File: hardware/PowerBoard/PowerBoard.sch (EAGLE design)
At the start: 136 parts, among them J1 CON-HRS-DM3AT, J2 CON-ZX62R-B-5P, J3 CON-FTSH-105-01-L-DV-K, J4 CON-S2B-PH-SM4-TB, J5 CON-PJ-102A, J6 CON-71436-2164, M1 MOUNT-HOLE3.3, M2 MOUNT-HOLE3.3, M3 MOUNT-HOLE3.3, M4 MOUNT-HOLE3.3, M5 FIDUCIAL1X2, M6 FIDUCIAL1X2, M7 FIDUCIAL1X2, M8 FIDUCIAL1X2, Q1 SI2323CDS, Q2 SI2312CDS, Q3 SI2333CDS, Q4 SI2333CDS, SW1 SWITCH-SPST, SW2 SWITCH-MS12ASG30, U1 LTC4361-2DC, U10 MAX9938FEUK, U11 MAX9938FEUK, U12 MAX9938FEUK, U13 STM32F10XCXT6, U14 LTC2942-1, U15 USBLC6-2, U2 LTC4085, U3 XC6220B331MR-G, U4 XC6220B331MR-G, U5 XC9236A15DMR-G, U6 MIC94043, U7 MAX9938FEUK, U8 MAX9938FEUK, U9 MAX9938FEUK, X1 ECX-2236, X2 ECX-31B

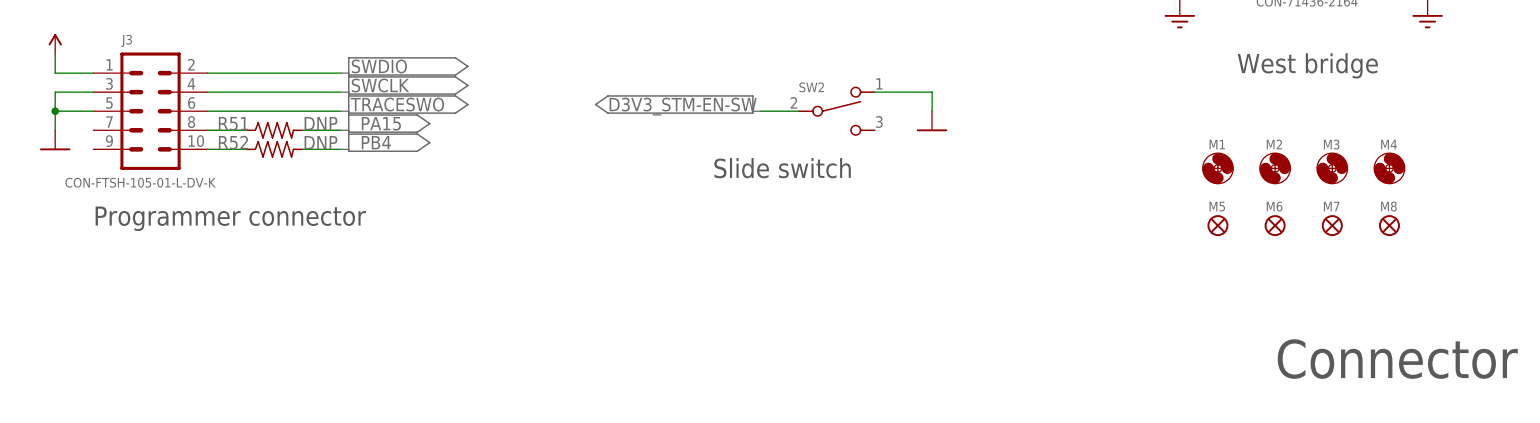
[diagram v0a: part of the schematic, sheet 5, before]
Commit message: Added USB D+ pull-up resistor and marked possible changes for Rev B.
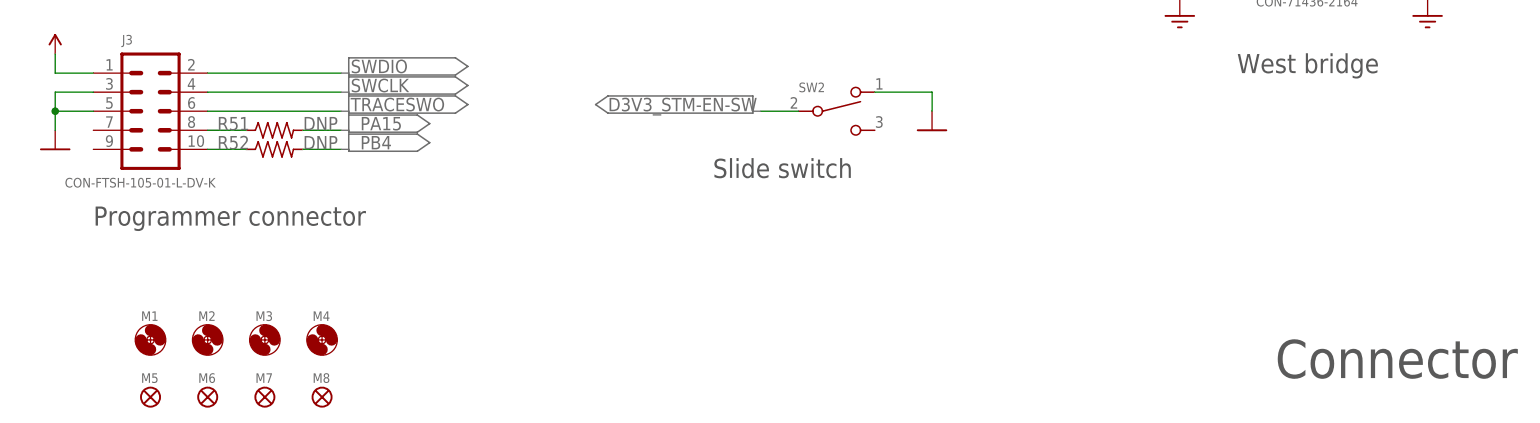
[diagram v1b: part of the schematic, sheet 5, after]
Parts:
- added R53: 1.5k, powerboard:R0603
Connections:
- net D3V3_STM: now also R53.2
- net USBDP: now also R53.1
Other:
- moved on the sheet: M1, M2, M3, M4, M5, M6, M7, M8
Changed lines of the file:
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@@
 <part name="M7" library="powerboard" deviceset="FIDUCIAL" device="1X2"/>
 <part name="M8" library="powerboard" deviceset="FIDUCIAL" device="1X2"/>
+<part name="R53" library="powerboard" deviceset="R" device="0603" value="1.5k"/>
+<part name="PORT81" library="powerboard" deviceset="PORT5" device=""/>
+<part name="U$66" library="powerboard" deviceset="D3V3_STM" device=""/>
 </parts>
 <sheets>
@@
 <text x="208.28" y="84.455" size="1.778" layer="97" rot="R180">60mV</text>
 <text x="186.69" y="91.44" size="1.778" layer="97">D3V3_STM</text>
+<rectangle x1="91.44" y1="129.54" x2="119.38" y2="144.78" layer="98"/>
+<rectangle x1="185.42" y1="134.62" x2="195.58" y2="154.94" layer="98"/>
 </plain>
 <instances>
@@
 <text x="223.52" y="87.63" size="1.778" layer="95" rot="R90">SUSP</text>
 <text x="213.36" y="87.63" size="1.778" layer="95" rot="R90">HPWR</text>
+<rectangle x1="-2.54" y1="60.96" x2="10.16" y2="104.14" layer="98"/>
 </plain>
 <instances>
@@
 <instance part="PORT138" gate="G$1" x="233.68" y="96.52" rot="R90"/>
 <instance part="U$65" gate="G$1" x="15.24" y="66.04"/>
+<instance part="R53" gate="G$1" x="5.08" y="83.82" rot="R90"/>
+<instance part="PORT81" gate="G$1" x="5.08" y="66.04" rot="R270"/>
+<instance part="U$66" gate="G$1" x="5.08" y="93.98" smashed="yes"/>
 </instances>
 <busses>
@@
 <pinref part="TP9" gate="G$1" pin="1"/>
 </segment>
+<segment>
+<wire x1="5.08" y1="86.36" x2="5.08" y2="93.98" width="0.1524" layer="91"/>
+<label x="-1.27" y="97.79" size="1.778" layer="95"/>
+<pinref part="U$66" gate="G$1" pin="D3V3_STM"/>
+<pinref part="R53" gate="G$1" pin="2"/>
+</segment>
 </net>
 <net name="VBAT" class="0">
@@
 <label x="233.68" y="87.63" size="1.778" layer="95" rot="R90"/>
 <pinref part="R44" gate="G$1" pin="2"/>
+</segment>
+</net>
+<net name="USBDP" class="0">
+<segment>
+<wire x1="5.08" y1="78.74" x2="5.08" y2="76.2" width="0.1524" layer="91"/>
+<label x="5.08" y="73.66" size="1.778" layer="95" rot="R270"/>
+<pinref part="R53" gate="G$1" pin="1"/>
 </segment>
 </net>
@@
 <text x="111.76" y="86.36" size="2.54" layer="97">Battery connector</text>
 <text x="115.57" y="46.99" size="2.54" layer="97">Slide switch</text>
+<rectangle x1="177.8" y1="53.34" x2="210.82" y2="157.48" layer="98"/>
 </plain>
 <instances>
@@
 <instance part="J4" gate="G$1" x="116.84" y="96.52"/>
 <instance part="J3" gate="G$1" x="40.64" y="55.88"/>
-<instance part="M1" gate="G$1" x="182.88" y="48.26"/>
-<instance part="M2" gate="G$1" x="190.5" y="48.26"/>
-<instance part="M3" gate="G$1" x="198.12" y="48.26"/>
-<instance part="M4" gate="G$1" x="205.74" y="48.26"/>
+<instance part="M1" gate="G$1" x="40.64" y="25.4"/>
+<instance part="M2" gate="G$1" x="48.26" y="25.4"/>
+<instance part="M3" gate="G$1" x="55.88" y="25.4"/>
+<instance part="M4" gate="G$1" x="63.5" y="25.4"/>
 <instance part="J5" gate="G$1" x="116.84" y="144.78"/>
 <instance part="SW2" gate="G$1" x="132.08" y="55.88"/>
@@
 <attribute name="VALUE" x="74.93" y="96.52" size="1.778" layer="96"/>
 </instance>
-<instance part="M5" gate="G$1" x="182.88" y="40.64"/>
-<instance part="M6" gate="G$1" x="190.5" y="40.64"/>
-<instance part="M7" gate="G$1" x="198.12" y="40.64"/>
-<instance part="M8" gate="G$1" x="205.74" y="40.64"/>
+<instance part="M5" gate="G$1" x="40.64" y="17.78"/>
+<instance part="M6" gate="G$1" x="48.26" y="17.78"/>
+<instance part="M7" gate="G$1" x="55.88" y="17.78"/>
+<instance part="M8" gate="G$1" x="63.5" y="17.78"/>
 </instances>
 <busses>

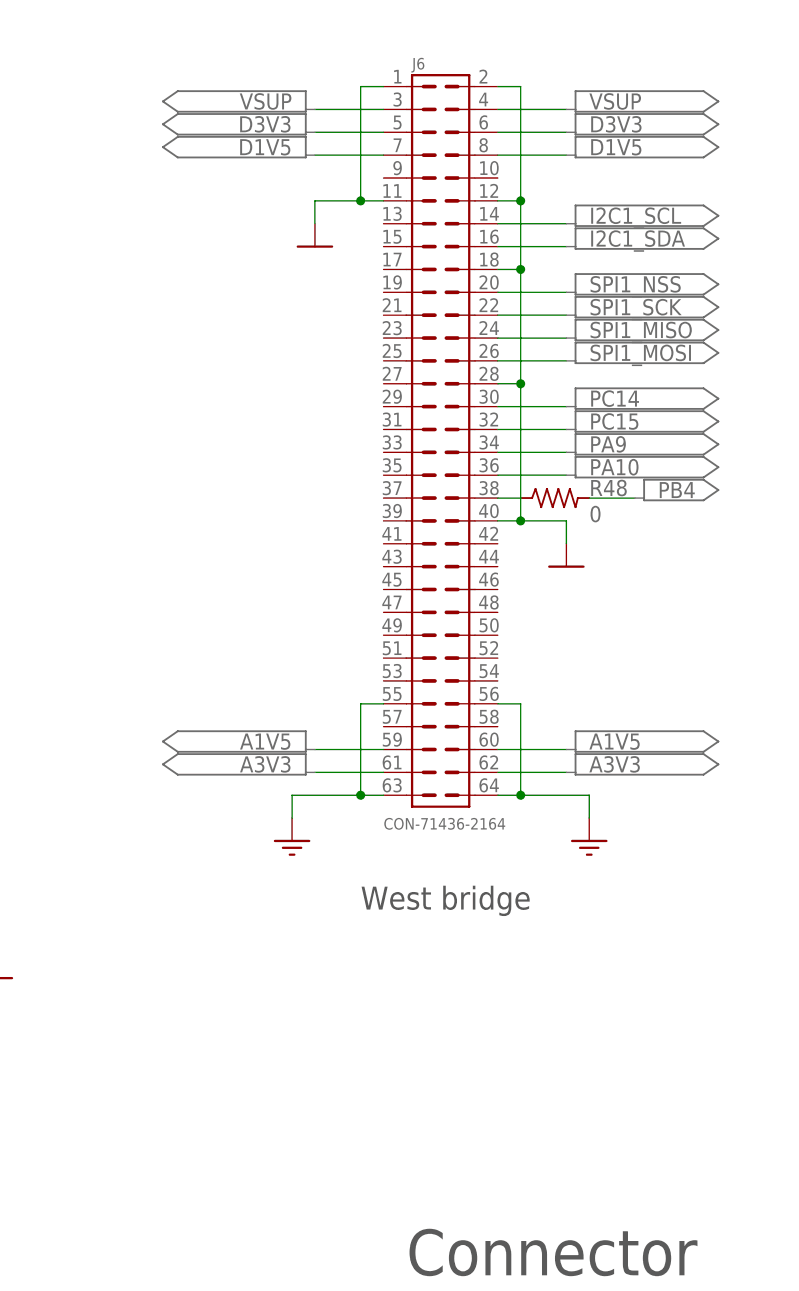
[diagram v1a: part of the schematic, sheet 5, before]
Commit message: - New 84 board-to-board connector (in schematic and routed) - info text on back corrected
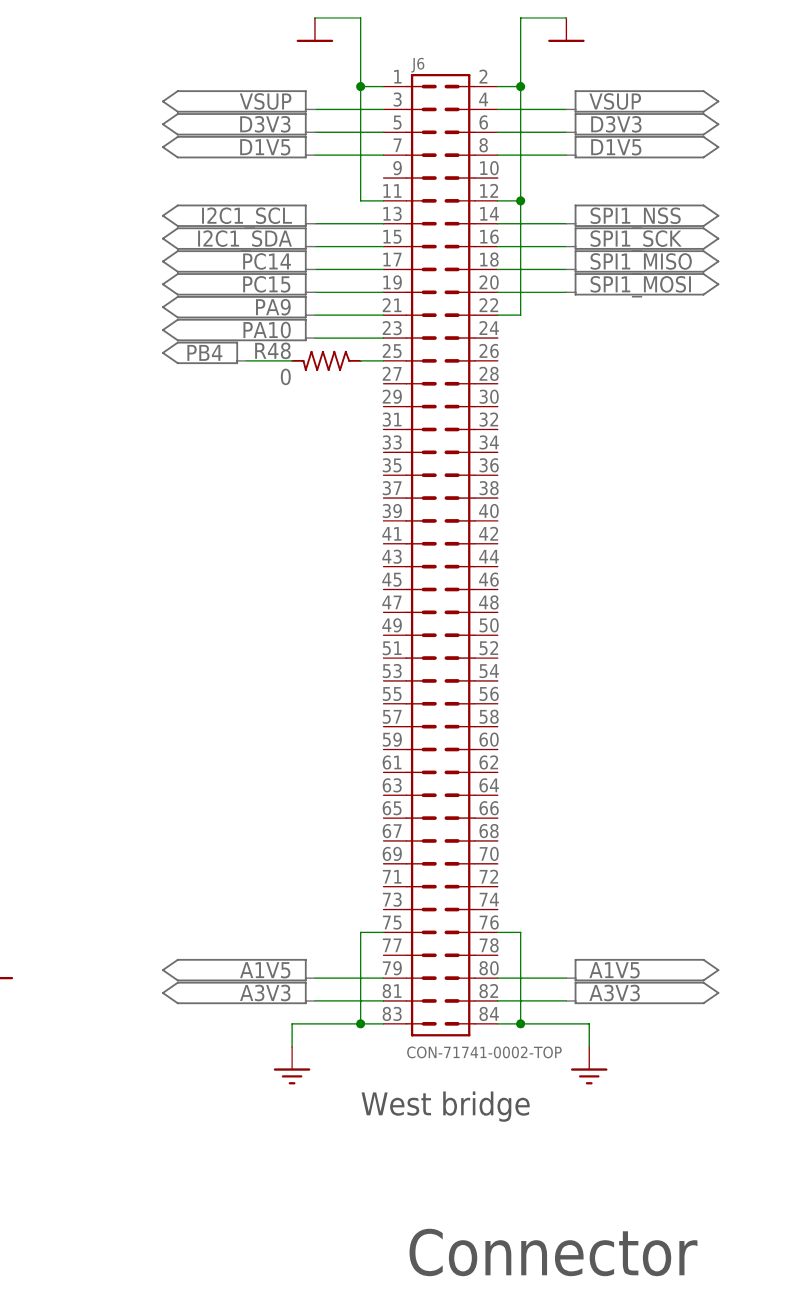
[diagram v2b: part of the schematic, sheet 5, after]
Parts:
- J6: value CON-71436-2164 -> CON-71741-0002-TOP; device powerboard:CON-71436-2164 -> powerboard:CON-71741-0002-TOP
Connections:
- net A1V5: now also J6.79, J6.80; no longer J6.59, J6.60
- net A3V3: now also J6.81, J6.82; no longer J6.61, J6.62
- net AGND: now also J6.75, J6.76, J6.83, J6.84; no longer J6.55, J6.56, J6.63, J6.64
- net DGND: now also J6.22; no longer J6.18, J6.28, J6.40
- net I2C1_SCL: now also J6.13; no longer J6.14
- net I2C1_SDA: now also J6.15; no longer J6.16
- net PA10: now also J6.23; no longer J6.36
- net PA9: now also J6.21; no longer J6.34
- net PB4-SF: now also J6.25; no longer J6.38
- net PC14: now also J6.17; no longer J6.30
- net PC15: now also J6.19; no longer J6.32
- net SPI1_MISO: now also J6.18; no longer J6.24
- net SPI1_MOSI: now also J6.20; no longer J6.26
- net SPI1_NSS: now also J6.14; no longer J6.20
- net SPI1_SCK: now also J6.16; no longer J6.22
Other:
- moved on the sheet: R48

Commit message: Minor cosmetic changes to 84-pin connector. Changed texts 'verifier' to 'reviewer'.
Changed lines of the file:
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@@
 <attribute name="PAGE4" value="Caps, Pulls and Misc"/>
 <attribute name="PAGE5" value="Connector"/>
+<attribute name="REVIEWER" value="Benjamin Babjak"/>
+<attribute name="REVIEWEREMAIL" value="benjamin.babjak@vanderbilt.edu"/>
 <attribute name="REVISION" value="B"/>
 <attribute name="TITLE" value="Power Board"/>
-<attribute name="VERIFIER" value="Peter Volgyesi"/>
-<attribute name="VERIFIEREMAIL" value="peter.volgyesi@vanderbilt.edu"/>
 </attributes>
 <variantdefs>
@@
 <parts>
 <part name="FRAME5" library="powerboard" deviceset="FRAME-LETTER" device=""/>
-<part name="AUTHOR-FIELD" library="powerboard" deviceset="FRATME-AUTHOR-FIELD" device=""/>
+<part name="AUTHOR-FIELD" library="powerboard" deviceset="FRAME-AUTHOR-FIELD" device=""/>
 <part name="TOC-FIELD" library="powerboard" deviceset="FRAME-TOC" device=""/>
 <part name="LOGO1" library="Logo" deviceset="LOGO-ISIS-600MIL" device="-10MM-CU"/>
@@
 <text x="161.29" y="20.32" size="2.54" layer="95" rot="MR0">&gt;AUTHOREMAIL</text>
 <text x="85.09" y="20.32" size="2.54" layer="95">&gt;AUTHOR</text>
-<text x="85.09" y="5.08" size="2.54" layer="95">&gt;VERIFIER</text>
-<text x="161.29" y="5.08" size="2.54" layer="95" rot="MR0">&gt;VERIFIEREMAIL</text>
+<text x="85.09" y="5.08" size="2.54" layer="95">&gt;REVIEWER</text>
+<text x="161.29" y="5.08" size="2.54" layer="95" rot="MR0">&gt;REVIEWEREMAIL</text>
 </plain>
 <instances>
@@
 <instance part="PORT87" gate="G$1" x="223.52" y="149.86"/>
 <instance part="PORT88" gate="G$1" x="223.52" y="147.32"/>
-<instance part="U$64" gate="G$1" x="208.28" y="157.48"/>
+<instance part="U$64" gate="G$1" x="210.82" y="111.76"/>
 <instance part="PORT94" gate="G$1" x="223.52" y="137.16"/>
 <instance part="PORT95" gate="G$1" x="223.52" y="134.62"/>
@@
 <instance part="PORT120" gate="G$1" x="223.52" y="50.8"/>
 <instance part="PORT89" gate="G$1" x="165.1" y="124.46" rot="MR0"/>
-<instance part="U$4" gate="G$1" x="180.34" y="157.48"/>
+<instance part="U$4" gate="G$1" x="177.8" y="111.76"/>
 <instance part="U15" gate="G$1" x="53.34" y="99.06"/>
 <instance part="J4" gate="G$1" x="116.84" y="96.52"/>
@@
 </segment>
 <segment>
-<wire x1="180.34" y1="160.02" x2="185.42" y2="160.02" width="0.1524" layer="91"/>
+<wire x1="177.8" y1="114.3" x2="177.8" y2="116.84" width="0.1524" layer="91"/>
+<pinref part="U$4" gate="G$1" pin="DGND"/>
 <wire x1="187.96" y1="152.4" x2="185.42" y2="152.4" width="0.1524" layer="91"/>
 <wire x1="185.42" y1="139.7" x2="185.42" y2="152.4" width="0.1524" layer="91"/>
-<wire x1="185.42" y1="160.02" x2="185.42" y2="152.4" width="0.1524" layer="91"/>
 <wire x1="185.42" y1="139.7" x2="187.96" y2="139.7" width="0.1524" layer="91"/>
-<pinref part="U$4" gate="G$1" pin="DGND"/>
 <pinref part="J6" gate="G$1" pin="1"/>
 <pinref part="J6" gate="G$1" pin="11"/>
-<junction x="185.42" y="152.4"/>
-</segment>
-<segment>
-<wire x1="208.28" y1="160.02" x2="203.2" y2="160.02" width="0.1524" layer="91"/>
+<wire x1="185.42" y1="139.7" x2="185.42" y2="116.84" width="0.1524" layer="91"/>
+<junction x="185.42" y="139.7"/>
+<wire x1="177.8" y1="116.84" x2="185.42" y2="116.84" width="0.1524" layer="91"/>
+</segment>
+<segment>
+<wire x1="210.82" y1="114.3" x2="210.82" y2="116.84" width="0.1524" layer="91"/>
+<wire x1="210.82" y1="116.84" x2="203.2" y2="116.84" width="0.1524" layer="91"/>
 <pinref part="U$64" gate="G$1" pin="DGND"/>
-<wire x1="203.2" y1="160.02" x2="203.2" y2="152.4" width="0.1524" layer="91"/>
+<wire x1="203.2" y1="116.84" x2="203.2" y2="127" width="0.1524" layer="91"/>
+<wire x1="203.2" y1="139.7" x2="203.2" y2="152.4" width="0.1524" layer="91"/>
 <wire x1="200.66" y1="152.4" x2="203.2" y2="152.4" width="0.1524" layer="91"/>
-<wire x1="203.2" y1="127" x2="203.2" y2="139.7" width="0.1524" layer="91"/>
-<wire x1="203.2" y1="139.7" x2="203.2" y2="152.4" width="0.1524" layer="91"/>
-<wire x1="200.66" y1="139.7" x2="203.2" y2="139.7" width="0.1524" layer="91"/>
-<junction x="203.2" y="139.7"/>
 <pinref part="J6" gate="G$1" pin="2"/>
 <pinref part="J6" gate="G$1" pin="12"/>
+<wire x1="200.66" y1="139.7" x2="203.2" y2="139.7" width="0.1524" layer="91"/>
+<wire x1="203.2" y1="127" x2="203.2" y2="139.7" width="0.1524" layer="91"/>
 <pinref part="J6" gate="G$1" pin="22"/>
 <wire x1="200.66" y1="127" x2="203.2" y2="127" width="0.1524" layer="91"/>
-<junction x="203.2" y="152.4"/>
-</segment>
-<segment>
+<junction x="203.2" y="139.7"/>
+<junction x="203.2" y="127"/>
+</segment>
+<segment>

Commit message: - Schematic updated
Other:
- moved on the sheet: R28, R29, R30, R31, R32, R33, R34, R35, R36, R37, R38, R39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

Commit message: - Logos changed - Small vias covered
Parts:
- removed LOGO2: LOGO-VANDERBILT-600MIL-10MM-CU, Logo:LOGO-VANDERBILT-600MIL-10MM-CU
- removed LOGO3: LOGO-MARMOTE-600MIL-10MM-CU, Logo:LOGO-MARMOTE-600MIL-10MM-CU
- removed LOGO4: LOGO-BATTERY-600MIL-10MM-CU, Logo:LOGO-BATTERY-600MIL-10MM-CU
- added LOGO5: LOGO-VANDERBILT-600MIL-10MM-AU, Logo:LOGO-VANDERBILT-600MIL-10MM-AU
- added LOGO6: LOGO-ISIS-600MIL-10MM-AU, Logo:LOGO-ISIS-600MIL-10MM-AU
- added LOGO7: LOGO-MARMOTE-600MIL-10MM-AU, Logo:LOGO-MARMOTE-600MIL-10MM-AU
- LOGO1: value LOGO-ISIS-600MIL-10MM-CU -> LOGO-BATTERY-600MIL-10MM-AU; device Logo:LOGO-ISIS-600MIL-10MM-CU -> Logo:LOGO-BATTERY-600MIL-10MM-AU
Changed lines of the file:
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@@
 <part name="AUTHOR-FIELD" library="powerboard" deviceset="FRAME-AUTHOR-FIELD" device=""/>
 <part name="TOC-FIELD" library="powerboard" deviceset="FRAME-TOC" device=""/>
-<part name="LOGO1" library="Logo" deviceset="LOGO-ISIS-600MIL" device="-10MM-CU"/>
-<part name="LOGO2" library="Logo" deviceset="LOGO-VANDERBILT-600MIL" device="-10MM-CU"/>
-<part name="LOGO3" library="Logo" deviceset="LOGO-MARMOTE-600MIL" device="-10MM-CU"/>
-<part name="LOGO4" library="Logo" deviceset="LOGO-BATTERY-600MIL" device="-10MM-CU"/>
 <part name="FRAME1" library="powerboard" deviceset="FRAME-LETTER" device="" value=""/>
 <part name="PORT5" library="powerboard" deviceset="PORT5" device=""/>
@@
 <part name="U$66" library="powerboard" deviceset="D3V3_STM" device=""/>
 <part name="J6" library="powerboard" deviceset="CON-71741" device="-0002-TOP"/>
+<part name="LOGO5" library="Logo" deviceset="LOGO-VANDERBILT-600MIL" device="-10MM-AU"/>
+<part name="LOGO6" library="Logo" deviceset="LOGO-ISIS-600MIL" device="-10MM-AU"/>
+<part name="LOGO7" library="Logo" deviceset="LOGO-MARMOTE-600MIL" device="-10MM-AU"/>
+<part name="LOGO1" library="Logo" deviceset="LOGO-BATTERY-600MIL" device="-10MM-AU"/>
 </parts>
 <sheets>
@@
 <instance part="AUTHOR-FIELD" gate="G$1" x="81.28" y="0"/>
 <instance part="TOC-FIELD" gate="G$1" x="0" y="0"/>
-<instance part="LOGO1" gate="G$1" x="104.14" y="60.96"/>
-<instance part="LOGO2" gate="G$1" x="78.74" y="60.96"/>
-<instance part="LOGO3" gate="G$1" x="129.54" y="60.96"/>
-<instance part="LOGO4" gate="G$1" x="154.94" y="60.96"/>
+<instance part="LOGO5" gate="G$1" x="78.74" y="60.96"/>
+<instance part="LOGO6" gate="G$1" x="104.14" y="60.96"/>
+<instance part="LOGO7" gate="G$1" x="129.54" y="60.96"/>
+<instance part="LOGO1" gate="G$1" x="154.94" y="60.96"/>
 </instances>
 <busses>
